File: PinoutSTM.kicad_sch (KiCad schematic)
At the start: 22 parts, among them IC1 STM32H7B0RBT6, J2 61300211121, J3 1761681-3, J4 Header male 1x05, J5 1792876, Q1 50V, SW1 Button Switch SPST-No, Y1 CC4V-T1A-32.768kHz-6pF-20PPM-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

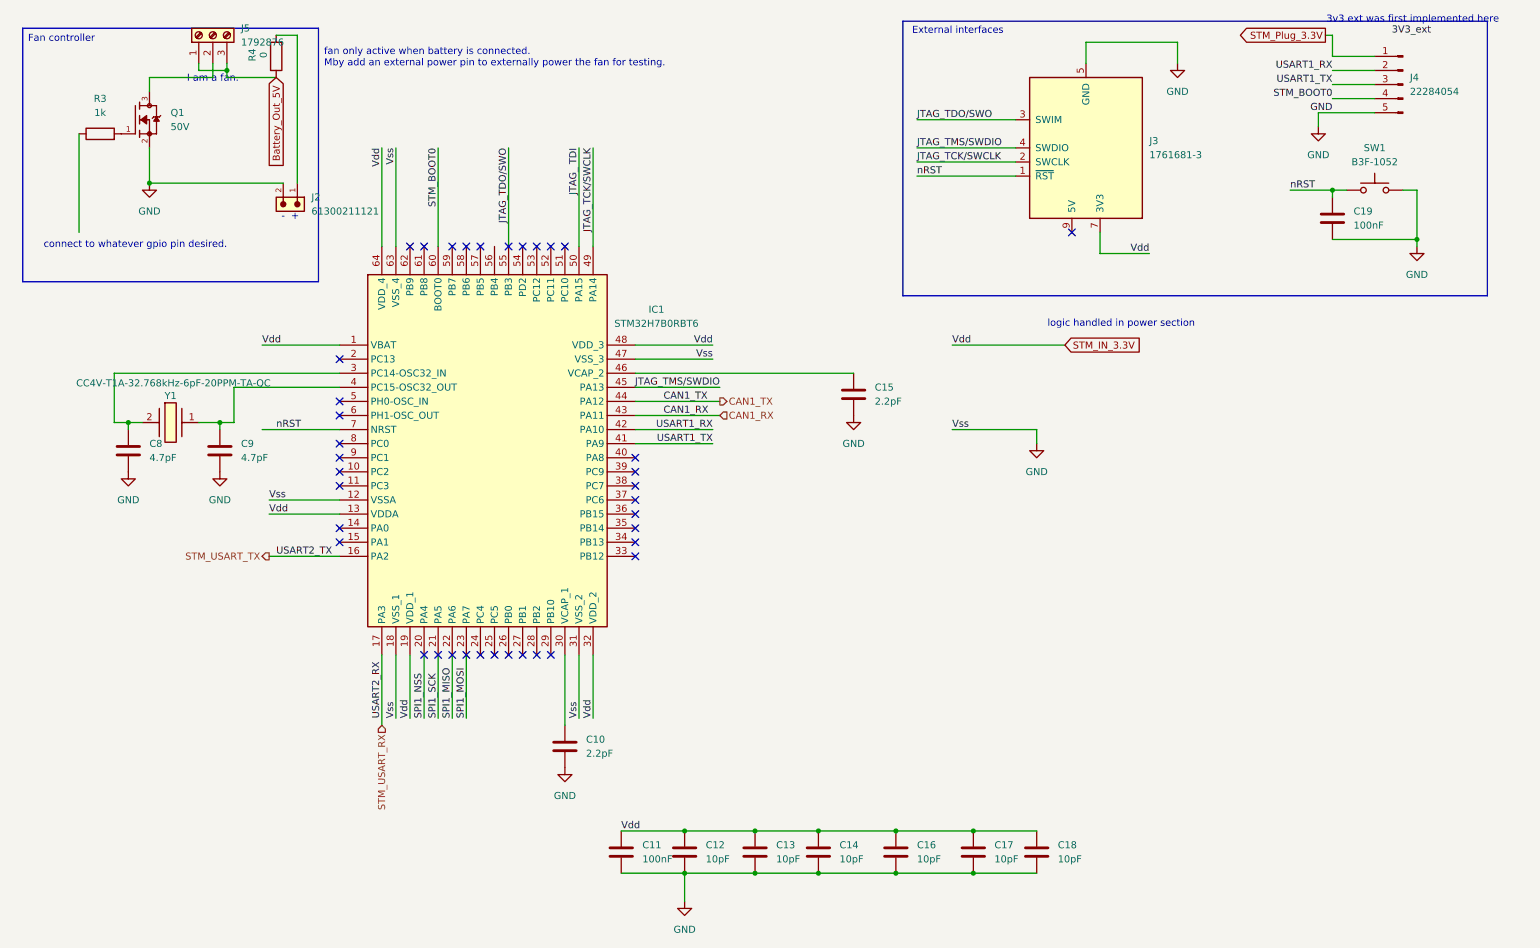
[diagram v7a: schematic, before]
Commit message: cleaned up some schematic problems
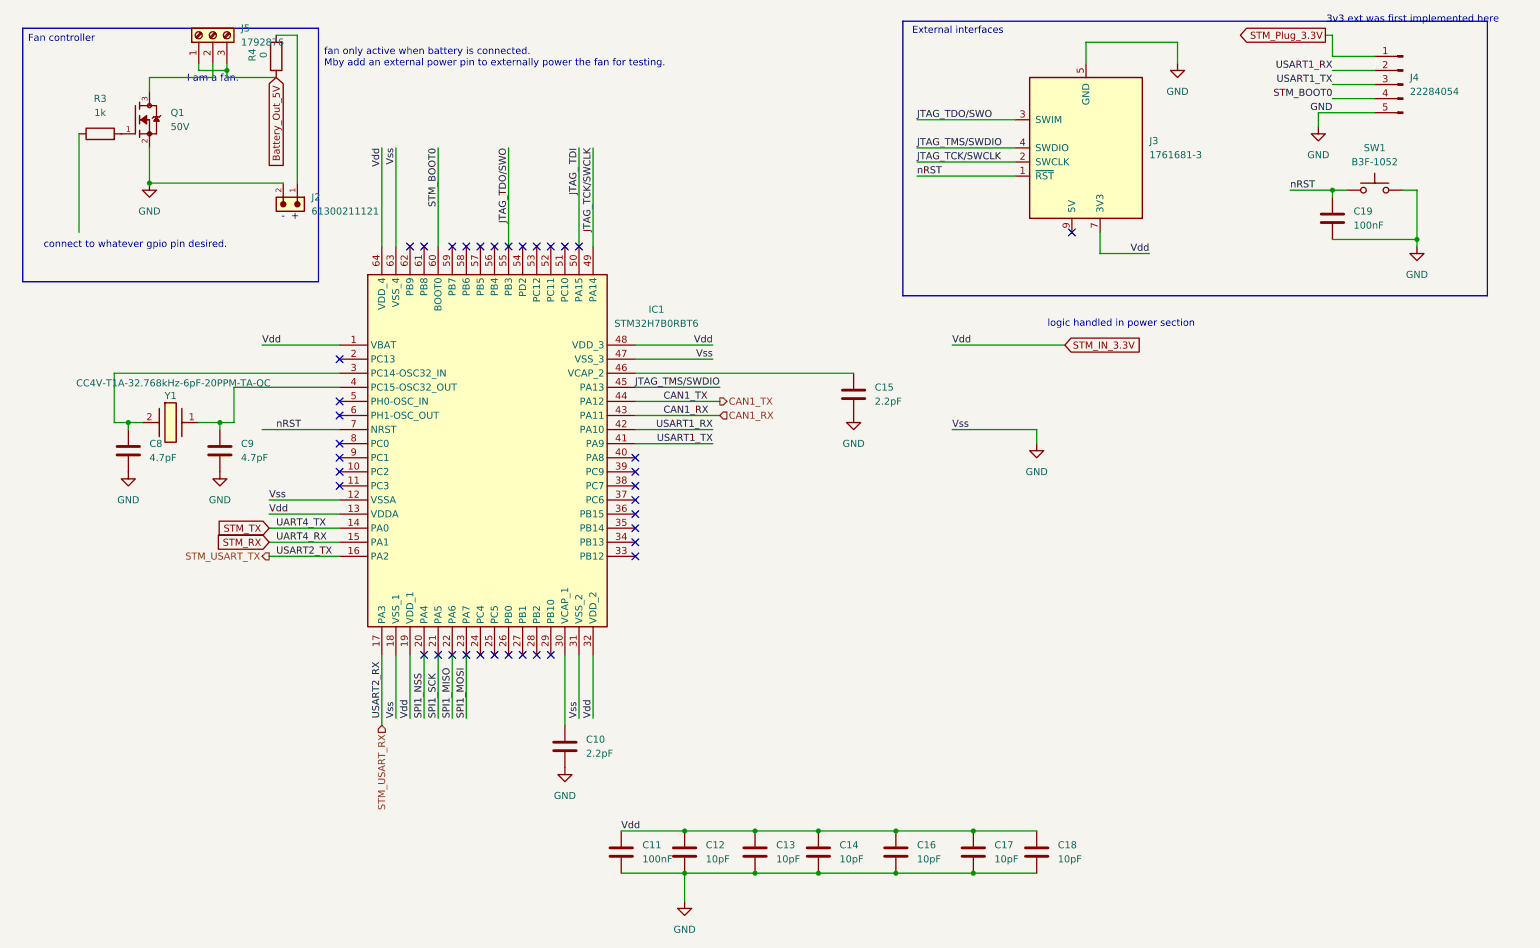
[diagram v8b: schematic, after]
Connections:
- net STM_TX: now reaches IC1.14 (PA0)
- net STM_RX: now reaches IC1.15 (PA1)
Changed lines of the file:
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@@
 	)
 	(no_connect
+		(at 115.57 54.61)
+	)
+	(no_connect
 		(at 90.17 128.27)
 	)
@@
 	)
 	(no_connect
+		(at 100.33 54.61)
+	)
+	(no_connect
 		(at 113.03 54.61)
 	)
@@
 	)
 	(no_connect
-		(at 72.39 107.95)
-	)
-	(no_connect
 		(at 110.49 128.27)
 	)
@@
 	)
 	(no_connect
-		(at 72.39 105.41)
-	)
-	(no_connect
 		(at 125.73 100.33)
 	)
@@
 	(wire
 		(pts
+			(xy 59.69 105.41) (xy 72.39 105.41)
+		)
+		(stroke
+			(width 0)
+			(type default)
+		)
+	)
+	(wire
+		(pts
 			(xy 209.55 55.88) (xy 218.44 55.88)
 		)
@@
 	(wire
 		(pts
+			(xy 59.69 107.95) (xy 72.39 107.95)
+		)
+		(stroke
+			(width 0)
+			(type default)
+		)
+	)
+	(wire
+		(pts
 			(xy 53.34 80.01) (xy 72.39 80.01)
 		)
@@
 		)
 	)
+	(label "UART4_TX"
+		(at 60.96 105.41 0)
+		(effects
+			(font
+				(size 1.27 1.27)
+			)
+			(justify left bottom)
+		)
+	)
 	(label "CAN1_TX"
 		(at 130.81 82.55 0)
@@
 		)
 	)
-	(label "3V3_ext"
-		(at 269.24 16.51 180)
-		(effects
-			(font
-				(size 1.27 1.27)
-			)
-			(justify right bottom)
-		)
-	)
 	(label "nRST"
 		(at 176.53 41.91 0)
@@
 		)
 	)
+	(label "UART4_RX"
+		(at 60.96 107.95 0)
+		(effects
+			(font
+				(size 1.27 1.27)
+			)
+			(justify left bottom)
+		)
+	)
 	(label "Vss"
 		(at 82.55 139.7 90)
@@
 		)
 	)
+	(global_label "STM_TX"
+		(shape input)
+		(at 59.69 105.41 180)
+		(fields_autoplaced yes)
+		(effects
+			(font
+				(size 1.27 1.27)
+			)
+			(justify right)
+		)
+		(property "Intersheetrefs" "${INTERSHEET_REFS}"
+			(at 49.9316 105.41 0)
+			(effects
+				(font
+					(size 1.27 1.27)
+				)
+				(justify right)
+				(hide yes)
+			)
+		)
+	)
 	(global_label "STM_Plug_3.3V"
 		(shape output)
@@
 			(effects
 				(font
+					(size 1.27 1.27)
+				)
+				(justify right)
+				(hide yes)
+			)
+		)
+	)
+	(global_label "STM_RX"
+		(shape input)
+		(at 59.69 107.95 180)
+		(fields_autoplaced yes)
+		(effects
+			(font
+				(size 1.27 1.27)
+			)
+			(justify right)
+		)
+		(property "Intersheetrefs" "${INTERSHEET_REFS}"
+			(at 49.6292 107.95 0)
+			(effects
+				(font
